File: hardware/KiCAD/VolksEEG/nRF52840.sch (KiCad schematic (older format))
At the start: 7 parts, among them J2 693061010911, U2 nRF52840-Feather-Sense-Board

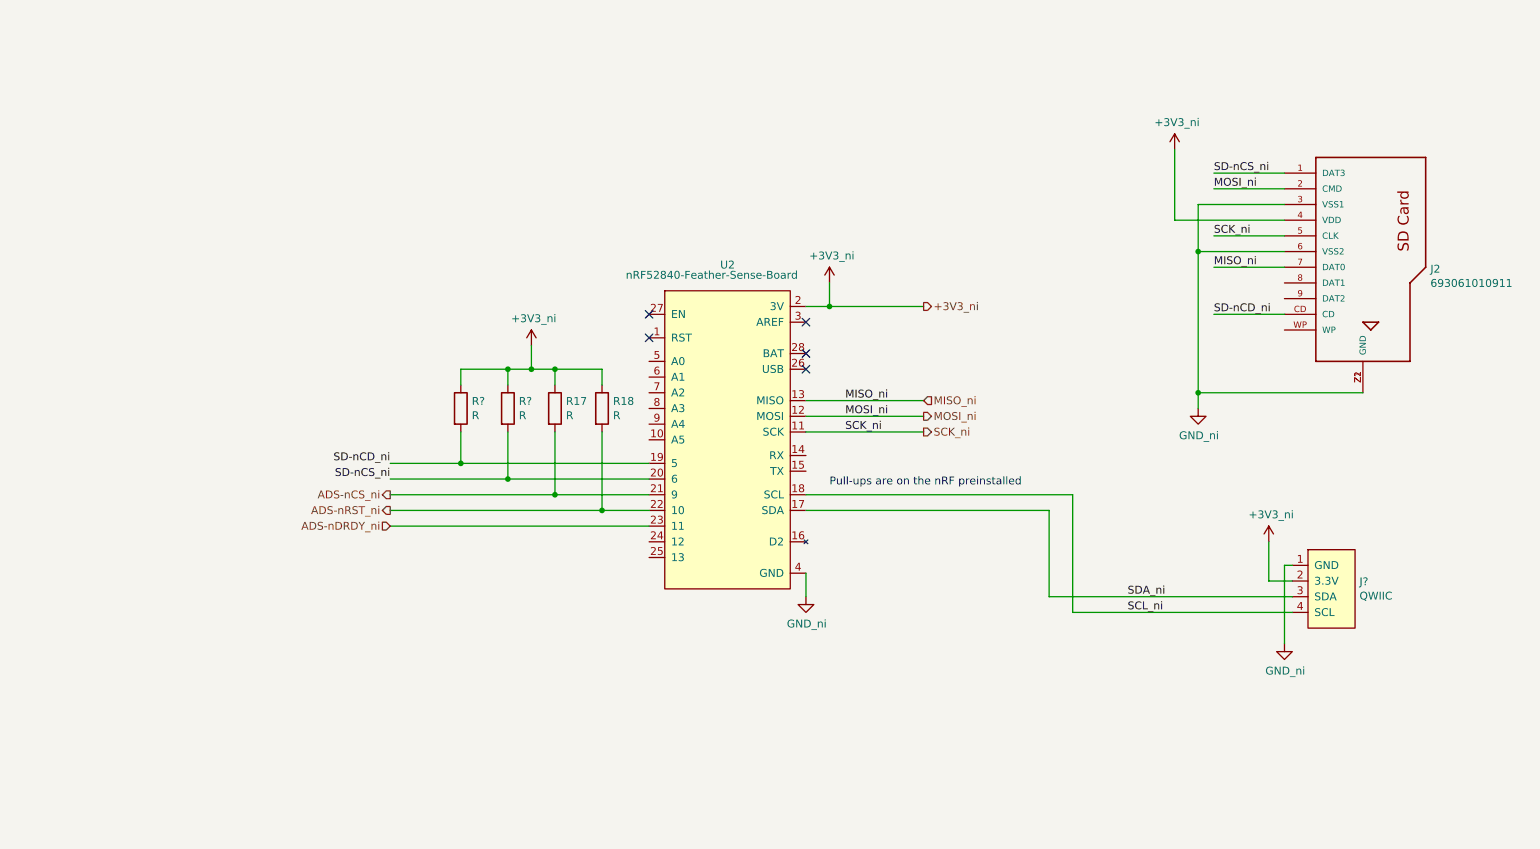
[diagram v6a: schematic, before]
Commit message: Added debugging bits to the NRF schematic sheet.
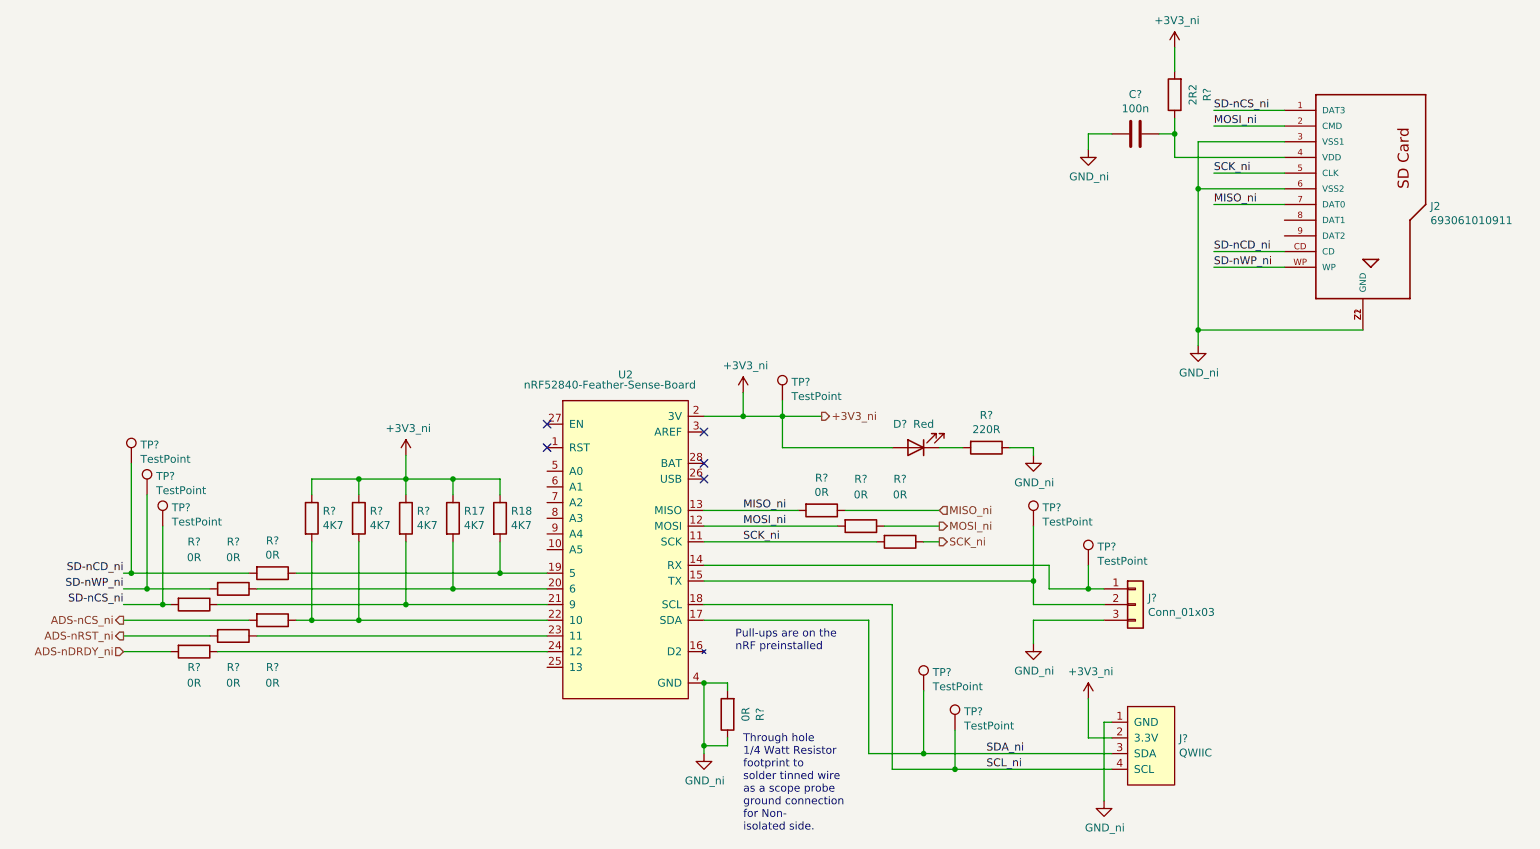
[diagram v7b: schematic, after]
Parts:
- added C?: 100n, symbol Device:C
- added D?: Red, symbol Device:LED
- added J?: Conn_01x03, symbol Connector_Generic:Conn_01x03
- added R?: 4K7, Resistor_SMD:R_0603_1608Metric_Pad0.98x0.95mm_HandSolder, symbol Device:R
- added R? (x10): 0R, symbol Device:R
- added R?: 2R2, symbol Device:R
- added R?: 220R, symbol Device:R
- added TP? (x8): TestPoint, symbol Connector:TestPoint
- R17, R18, R? (x2): value R -> 4K7
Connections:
- net +3V3: now also D?.2 (A), R?.1, R?.2, TP?.1; no longer J2.4 (VDD)
- net ADS-nCS_ni: now also R?.2; no longer R17.2, U2.21 (9)
- net ADS-nDRDY_ni: now also R?.2; no longer U2.23 (11)
- net ADS-nRST_ni: now also R?.2; no longer R18.2, U2.22 (10)
- net GND: now also C?.2, J?.3 (Pin_3), R?.1, R?.1, R?.2
- net MISO_ni: now also R?.1, R?.2
- net MOSI_ni: now also R?.1, R?.2
- net SCK_ni: now also R?.1, R?.2
- net SCL_ni: now also TP?.1
- net SD-nCD_ni: now also R?.2, TP?.1; no longer R?.2, U2.19 (5)
- net SD-nCS_ni: now also R?.2, TP?.1; no longer R?.2, U2.20 (6)
- net SDA_ni: now also TP?.1
- net at U2.14 (RX): now also J?.1 (Pin_1), TP?.1
- net at U2.15 (TX): now also J?.2 (Pin_2), TP?.1
- net at U2.24 (12): now also R?.1
- net SD-nWP_ni: now reaches J2.WP
- net SD-nWP_ni: now also R?.2, TP?.1
- new net: R18.2, R?.1, U2.19 (5)
- new net: R17.2, R?.1, U2.20 (6)
- new net: R?.1, R?.2, U2.21 (9)
- new net: R?.1, R?.2, R?.2, U2.22 (10)
- new net: R?.1, U2.23 (11)
- new net: C?.1, J2.4 (VDD), R?.1
- new net: D?.1 (K), R?.2
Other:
- note added: "Pull-ups are on the \nnRF preinstalled"
- note added: "Through hole \n1/4 Watt Resistor \nfootprint to \nsolder tinned wire \nas a scope probe \nground connection\nfor Non-\nisolated side."
- note removed: "Pull-ups are on the nRF preinstalled"
- moved on the sheet: J2, J?, R17, R18, R?, U2

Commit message: Added debugging bits to more schematic sheets.
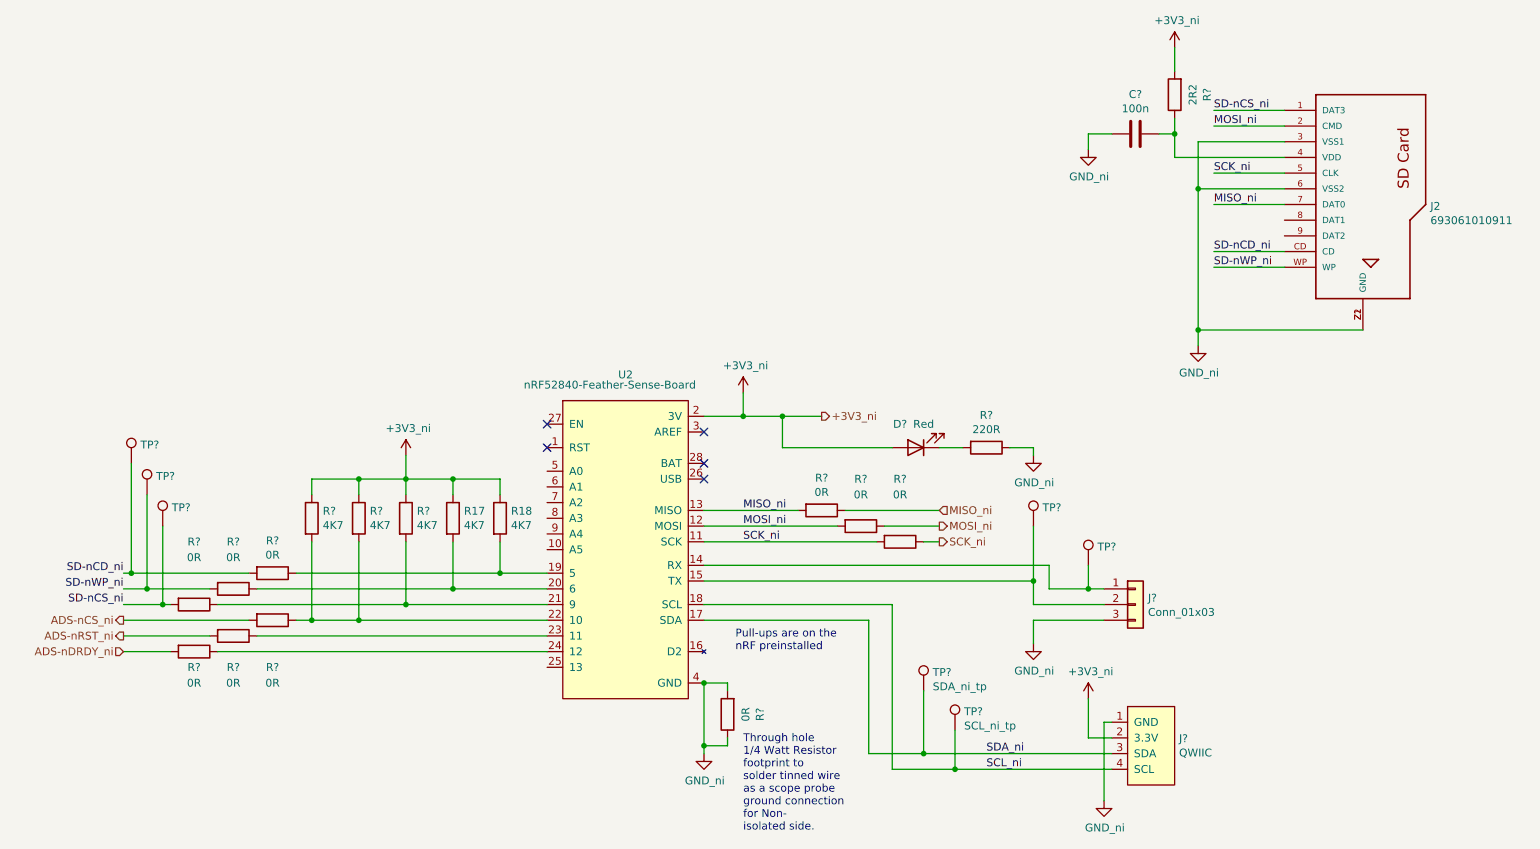
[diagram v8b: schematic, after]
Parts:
- removed TP?: TestPoint, symbol Connector:TestPoint
- TP?: value TestPoint -> SCL_ni_tp
- TP?: value TestPoint -> SDA_ni_tp
- TP?: value TestPoint -> Rx_ni_tp
- TP?: value TestPoint -> Tx_ni_tp
- TP?: value TestPoint -> SD-nCS_ni_tp
- TP?: value TestPoint -> SD-nWP_ni_tp
- TP?: value TestPoint -> SD-nCD_ni_tp
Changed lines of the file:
@@
-$Comp
-L Connector:TestPoint TP?
-U 1 1 61E155A2
-P 5900 3300
-F 0 "TP?" H 5958 3418 50  0000 L CNN
-F 1 "TestPoint" H 5958 3327 50  0000 L CNN
-F 2 "" H 6100 3300 50  0001 C CNN
-F 3 "~" H 6100 3300 50  0001 C CNN
-	1    5900 3300
-	1    0    0    -1
-$EndComp
 $Comp
 L Connector:TestPoint TP?
@@
 P 7000 5400
 F 0 "TP?" H 7058 5518 50  0000 L CNN
-F 1 "TestPoint" H 7058 5427 50  0000 L CNN
+F 1 "SCL_ni_tp" H 7058 5427 50  0000 L CNN
 F 2 "" H 7200 5400 50  0001 C CNN
 F 3 "~" H 7200 5400 50  0001 C CNN
@@
 P 6800 5150
 F 0 "TP?" H 6858 5268 50  0000 L CNN
-F 1 "TestPoint" H 6858 5177 50  0000 L CNN
+F 1 "SDA_ni_tp" H 6858 5177 50  0000 L CNN
 F 2 "" H 7000 5150 50  0001 C CNN
 F 3 "~" H 7000 5150 50  0001 C CNN
@@
 Wire Wire Line
 	7000 5650 8000 5650
-Wire Wire Line
-	5900 3300 5900 3400
 Connection ~ 5900 3400
 Wire Wire Line
@@
 P 7850 4350
 F 0 "TP?" H 7908 4468 50  0000 L CNN
-F 1 "TestPoint" H 7908 4377 50  0000 L CNN
+F 1 "Rx_ni_tp" H 7908 4377 50  0001 L CNN
 F 2 "" H 8050 4350 50  0001 C CNN
 F 3 "~" H 8050 4350 50  0001 C CNN
@@
 P 7500 4100
 F 0 "TP?" H 7558 4218 50  0000 L CNN
-F 1 "TestPoint" H 7558 4127 50  0000 L CNN
+F 1 "Tx_ni_tp" H 7558 4127 50  0001 L CNN
 F 2 "" H 7700 4100 50  0001 C CNN
 F 3 "~" H 7700 4100 50  0001 C CNN
@@
 P 1950 4100
 F 0 "TP?" H 2008 4218 50  0000 L CNN
-F 1 "TestPoint" H 2008 4127 50  0000 L CNN
+F 1 "SD-nCS_ni_tp" H 2008 4127 50  0001 L CNN
 F 2 "" H 2150 4100 50  0001 C CNN
 F 3 "~" H 2150 4100 50  0001 C CNN
@@
 P 1850 3900
 F 0 "TP?" H 1908 4018 50  0000 L CNN
-F 1 "TestPoint" H 1908 3927 50  0000 L CNN
+F 1 "SD-nWP_ni_tp" H 1908 3927 50  0001 L CNN
 F 2 "" H 2050 3900 50  0001 C CNN
 F 3 "~" H 2050 3900 50  0001 C CNN
@@
 P 1750 3700
 F 0 "TP?" H 1808 3818 50  0000 L CNN
-F 1 "TestPoint" H 1808 3727 50  0000 L CNN
+F 1 "SD-nCD_ni_tp" H 1808 3727 50  0001 L CNN
 F 2 "" H 1950 3700 50  0001 C CNN
 F 3 "~" H 1950 3700 50  0001 C CNN
